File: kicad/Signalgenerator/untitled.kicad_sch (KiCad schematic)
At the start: 1 part, among them U8 LT3462ES6-TRPBF

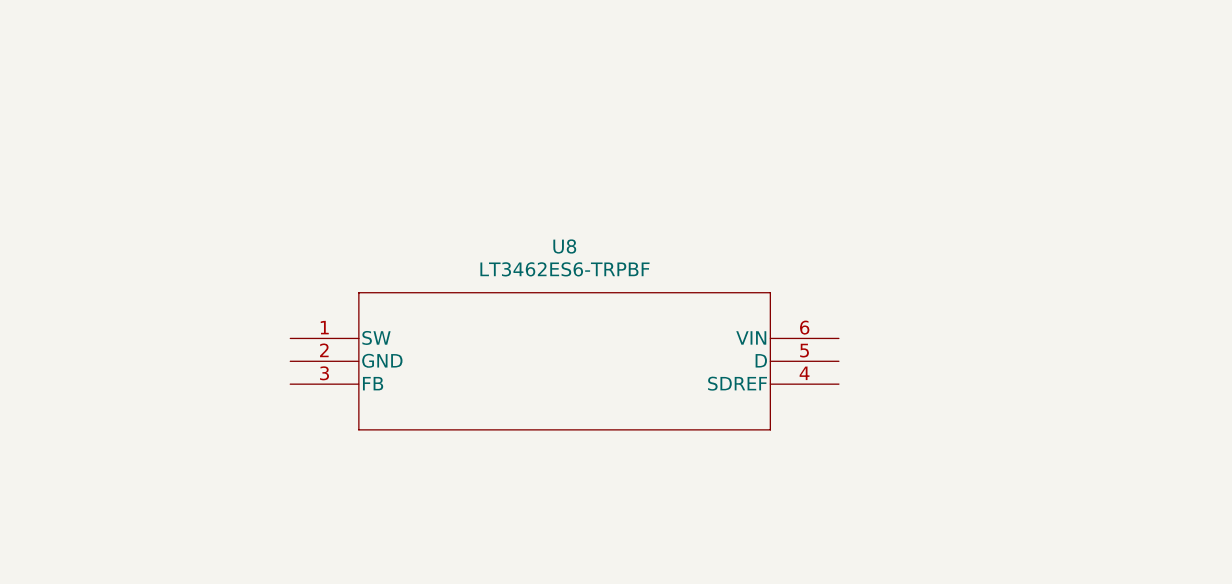
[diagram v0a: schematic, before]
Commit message: Platine layout angefangen. Probleme mit Überkreuzungen.
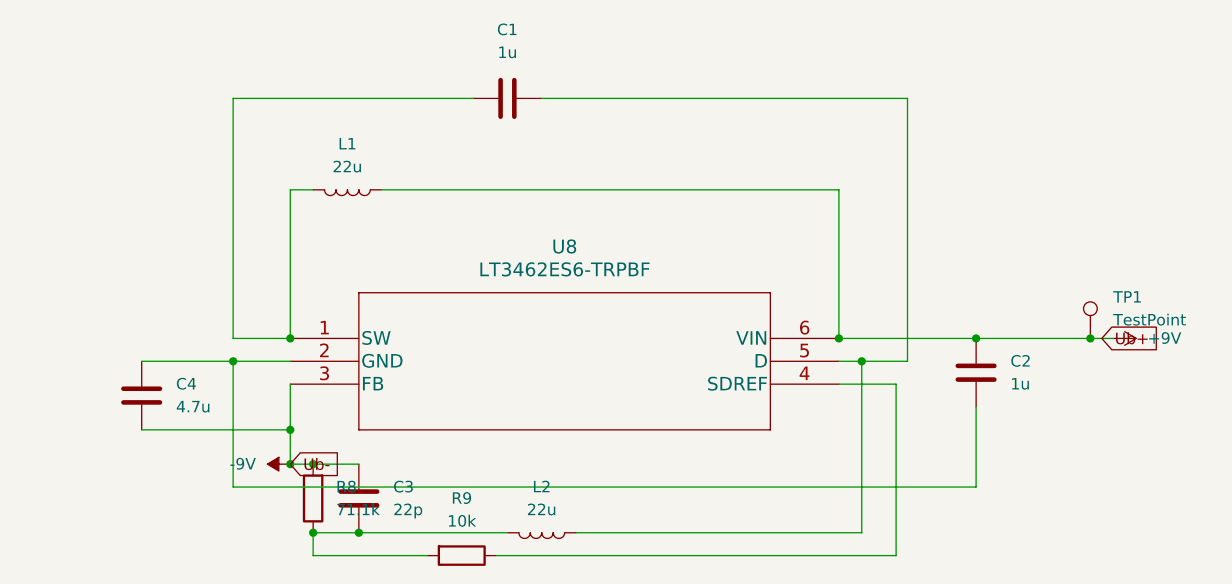
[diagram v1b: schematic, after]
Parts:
- added C1, C2: 1u, Capacitor_SMD:C_0603_1608Metric_Pad1.08x0.95mm_HandSolder, symbol Device:C
- added C3: 22p, Capacitor_SMD:C_0603_1608Metric_Pad1.08x0.95mm_HandSolder, symbol Device:C
- added C4: 4.7u, Capacitor_SMD:C_0603_1608Metric_Pad1.08x0.95mm_HandSolder, symbol Device:C
- added L1, L2: 22u, Inductor_SMD:L_0603_1608Metric_Pad1.05x0.95mm_HandSolder, symbol Device:L
- added R8: 71.1k, Resistor_SMD:R_0805_2012Metric_Pad1.20x1.40mm_HandSolder, symbol Device:R
- added R9: 10k, Resistor_SMD:R_0805_2012Metric_Pad1.20x1.40mm_HandSolder, symbol Device:R
- added TP1: TestPoint, TestPoint:TestPoint_THTPad_2.0x2.0mm_Drill1.0mm, symbol Connector:TestPoint
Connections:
- net at U8.1 (SW): now also C1.2, L1.2
- net at U8.2 (GND): now also C2.1, C4.2
- net -9V: now reaches U8.3 (FB)
- net -9V: now also C3.2, C4.1, R8.2
- net at U8.4 (SDREF): now also R9.1
- net at U8.5 (D): now also C1.1, L2.1
- net +9V: now reaches U8.6 (VIN)
- net +9V: now also C2.2, L1.1, TP1.1
- new net: C3.1, L2.2, R8.1, R9.2

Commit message: kleine änderungen
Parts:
- added C5: 2.2u, Capacitor_SMD:C_0603_1608Metric_Pad1.08x0.95mm_HandSolder, symbol Device:C
- C4: value 4.7u -> 2.2u
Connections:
- net -9V: now also C5.1
- net at C2.1, C4.2, U8.2 (GND): now also C5.2
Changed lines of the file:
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@@
+	)
+	(junction
+		(at 85.09 90.17)
+		(diameter 0)
+		(color 0 0 0 0)
+	)
+	(junction
+		(at 85.09 97.79)
+		(diameter 0)
+		(color 0 0 0 0)
 	)
 	(junction
@@
 	(wire
 		(pts
+			(xy 85.09 90.17) (xy 88.9 90.17)
+		)
+		(stroke
+			(width 0)
+			(type default)
+		)
+	)
+	(wire
+		(pts
 			(xy 184.15 87.63) (xy 186.69 87.63)
 		)
@@
 	(wire
 		(pts
-			(xy 78.74 90.17) (xy 88.9 90.17)
+			(xy 85.09 97.79) (xy 95.25 97.79)
+		)
+		(stroke
+			(width 0)
+			(type default)
+		)
+	)
+	(wire
+		(pts
+			(xy 78.74 90.17) (xy 85.09 90.17)
 		)
 		(stroke
@@
 	(wire
 		(pts
-			(xy 78.74 97.79) (xy 95.25 97.79)
+			(xy 78.74 97.79) (xy 85.09 97.79)
 		)
 		(stroke
@@
 			)
 		)
-		(property "Value" "4.7u"
+		(property "Value" "2.2u"
 			(at 82.55 95.2499 0)
 			(effects
@@
 					(unit 1)
 				)
+			)
+		)
+	)
+	(symbol
+		(lib_id "Device:C")
+		(at 85.09 93.98 180)
+		(unit 1)
+		(exclude_from_sim no)
+		(in_bom yes)
+		(on_board yes)
+		(dnp no)
+		(fields_autoplaced yes)
+		(property "Reference" "C5"
+			(at 88.9 92.7099 0)
+			(effects
+				(font
+					(size 1.27 1.27)
+				)
+				(justify right)
+			)
+		)
+		(property "Value" "2.2u"
+			(at 88.9 95.2499 0)
+			(effects
+				(font
+					(size 1.27 1.27)
+				)
+				(justify right)
+			)
+		)
+		(property "Footprint" "Capacitor_SMD:C_0603_1608Metric_Pad1.08x0.95mm_HandSolder"
+			(at 84.1248 90.17 0)
+			(effects
+				(font
+					(size 1.27 1.27)
+				)
+				(hide yes)
+			)
+		)
+		(property "Datasheet" "~"
+			(at 85.09 93.98 0)
+			(effects
+				(font
+					(size 1.27 1.27)
+				)
+				(hide yes)
+			)
+		)
+		(property "Description" "Unpolarized capacitor"
+			(at 85.09 93.98 0)
+			(effects
+				(font
+					(size 1.27 1.27)
+				)
+				(hide yes)
+			)
+		)
+		(pin "1"
+		)
+		(pin "2"
+		)
+		(instances
+			(project "Signalgenerator"
+				(path "/8862b47a-3c46-4bfb-a99b-c8e005d2d344/03138af8-b262-40e9-ad79-63335365d49e"
+					(reference "C5")
+					(unit 1)
+				)

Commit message: layout zwischenstand
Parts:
- added C21: 0.1u, Capacitor_SMD:C_0603_1608Metric_Pad1.08x0.95mm_HandSolder, symbol Device:C
- added J1, J2: Conn_01x01, Connector_PinHeader_2.54mm:PinHeader_1x01_P2.54mm_Vertical, symbol Connector_Generic:Conn_01x01
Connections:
- net +9V: now also J1.1 (Pin_1)
- net -9V: now also C21.2
- net GND: now reaches C2.1, C4.2, C5.2, U8.2 (GND)
- net GND: now also C21.1, J2.1 (Pin_1)

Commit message: schaltplan angepasst
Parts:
- added C7, C9: C, Capacitor_SMD:C_0603_1608Metric_Pad1.08x0.95mm_HandSolder, symbol Device:C
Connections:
- net +9V: now also C7.1, C9.1
- net -9V: now also C7.2, C9.2
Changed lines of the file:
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@@
 	(paper "A4")
 	(junction
+		(at 176.53 87.63)
+		(diameter 0)
+		(color 0 0 0 0)
+	)
+	(junction
 		(at 78.74 90.17)
 		(diameter 0)
@@
 	)
 	(junction
+		(at 180.34 87.63)
+		(diameter 0)
+		(color 0 0 0 0)
+	)
+	(junction
 		(at 95.25 97.79)
 		(diameter 0)
@@
 	(wire
 		(pts
+			(xy 180.34 87.63) (xy 184.15 87.63)
+		)
+		(stroke
+			(width 0)
+			(type default)
+		)
+	)
+	(wire
+		(pts
 			(xy 95.25 97.79) (xy 95.25 92.71)
 		)
@@
 	(wire
 		(pts
-			(xy 179.07 87.63) (xy 184.15 87.63)
+			(xy 179.07 87.63) (xy 180.34 87.63)
 		)
 		(stroke
@@
 	(wire
 		(pts
-			(xy 171.45 87.63) (xy 179.07 87.63)
+			(xy 171.45 87.63) (xy 176.53 87.63)
 		)
 		(stroke
@@
 	(wire
 		(pts
+			(xy 176.53 95.25) (xy 180.34 95.25)
+		)
+		(stroke
+			(width 0)
+			(type default)
+		)
+	)
+	(wire
+		(pts
 			(xy 171.45 104.14) (xy 88.9 104.14)
 		)
@@
 	(wire
 		(pts
+			(xy 176.53 87.63) (xy 179.07 87.63)
+		)
+		(stroke
+			(width 0)
+			(type default)
+		)
+	)
+	(wire
+		(pts
 			(xy 163.83 90.17) (xy 158.75 90.17)
 		)
@@
 			(width 0)
 			(type default)
+		)
+	)
+	(global_label "Ub-"
+		(shape input)
+		(at 180.34 95.25 0)
+		(fields_autoplaced yes)
+		(effects
+			(font
+				(size 1.27 1.27)
+			)
+			(justify left)
+		)
+		(property "Intersheetrefs" "${INTERSHEET_REFS}"
+			(at 187.3771 95.25 0)
+			(effects
+				(font
+					(size 1.27 1.27)
+				)
+				(justify left)
+				(hide yes)
+			)
 		)
 	)
@@
 	)
 	(symbol
+		(lib_id "Device:C")
+		(at 180.34 91.44 0)
+		(unit 1)
+		(exclude_from_sim no)
+		(in_bom yes)
+		(on_board yes)
+		(dnp no)
+		(fields_autoplaced yes)
+		(property "Reference" "C9"
+			(at 184.15 90.1699 0)
+			(effects
+				(font
+					(size 1.27 1.27)
+				)
+				(justify left)
+			)
+		)
+		(property "Value" "C"
+			(at 184.15 92.7099 0)
+			(effects
+				(font
+					(size 1.27 1.27)
+				)
+				(justify left)
+			)
+		)
+		(property "Footprint" "Capacitor_SMD:C_0603_1608Metric_Pad1.08x0.95mm_HandSolder"
+			(at 181.3052 95.25 0)
+			(effects
+				(font
+					(size 1.27 1.27)
+				)
+				(hide yes)
+			)
+		)
+		(property "Datasheet" "~"
+			(at 180.34 91.44 0)
+			(effects
+				(font
+					(size 1.27 1.27)
+				)
+				(hide yes)
+			)
+		)
+		(property "Description" "Unpolarized capacitor"
+			(at 180.34 91.44 0)
+			(effects
+				(font
+					(size 1.27 1.27)
+				)
+				(hide yes)
+			)
+		)
+		(pin "2"
+		)
+		(pin "1"
+		)
+		(instances
+			(project "Signalgenerator"
+				(path "/8862b47a-3c46-4bfb-a99b-c8e005d2d344/03138af8-b262-40e9-ad79-63335365d49e"
+					(reference "C9")
+					(unit 1)
+				)
+			)
+		)
+	)
+	(symbol
 		(lib_id "power:GND")
 		(at 68.58 90.17 0)
@@
 					(unit 1)
 				)
+			)
+		)
+	)
+	(symbol
+		(lib_id "Device:C")
+		(at 176.53 91.44 0)
+		(unit 1)
+		(exclude_from_sim no)
+		(in_bom yes)
+		(on_board yes)
+		(dnp no)
+		(fields_autoplaced yes)
+		(property "Reference" "C7"
+			(at 180.34 90.1699 0)
+			(effects
+				(font
+					(size 1.27 1.27)
+				)
+				(justify left)
+			)
+		)
+		(property "Value" "C"
+			(at 180.34 92.7099 0)
+			(effects
+				(font
+					(size 1.27 1.27)
+				)
+				(justify left)
+			)
+		)
+		(property "Footprint" "Capacitor_SMD:C_0603_1608Metric_Pad1.08x0.95mm_HandSolder"
+			(at 177.4952 95.25 0)
+			(effects
+				(font
+					(size 1.27 1.27)
+				)
+				(hide yes)
+			)
+		)
+		(property "Datasheet" "~"
+			(at 176.53 91.44 0)
+			(effects
+				(font
+					(size 1.27 1.27)
+				)
+				(hide yes)
+			)
+		)
+		(property "Description" "Unpolarized capacitor"
+			(at 176.53 91.44 0)
+			(effects
+				(font
+					(size 1.27 1.27)
+				)
+				(hide yes)
+			)
+		)
+		(pin "1"
+		)
+		(pin "2"
+		)
+		(instances
+			(project "Signalgenerator"
+				(path "/8862b47a-3c46-4bfb-a99b-c8e005d2d344/03138af8-b262-40e9-ad79-63335365d49e"
+					(reference "C7")
+					(unit 1)
+				)
